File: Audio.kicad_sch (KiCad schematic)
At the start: 8 parts, among them T1 1:1 600R Audio, T2 1:1 600R Audio

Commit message: Assign footprints to devices
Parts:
- C10, C7, C8, C9: footprint (none) -> Capacitor_SMD:C_0201_0603Metric
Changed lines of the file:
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@@
 			)
 		)
-		(property "Footprint" ""
+		(property "Footprint" "Capacitor_SMD:C_0201_0603Metric"
 			(at 162.2552 106.68 0)
 			(effects
@@
 			)
 		)
-		(property "Footprint" ""
+		(property "Footprint" "Capacitor_SMD:C_0201_0603Metric"
 			(at 163.5252 46.99 0)
 			(effects
@@
 			)
 		)
-		(property "Footprint" ""
+		(property "Footprint" "Capacitor_SMD:C_0201_0603Metric"
 			(at 82.55 113.3348 0)
 			(effects
@@
 			)
 		)
-		(property "Footprint" ""
+		(property "Footprint" "Capacitor_SMD:C_0201_0603Metric"
 			(at 97.79 57.15 0)
 			(effects

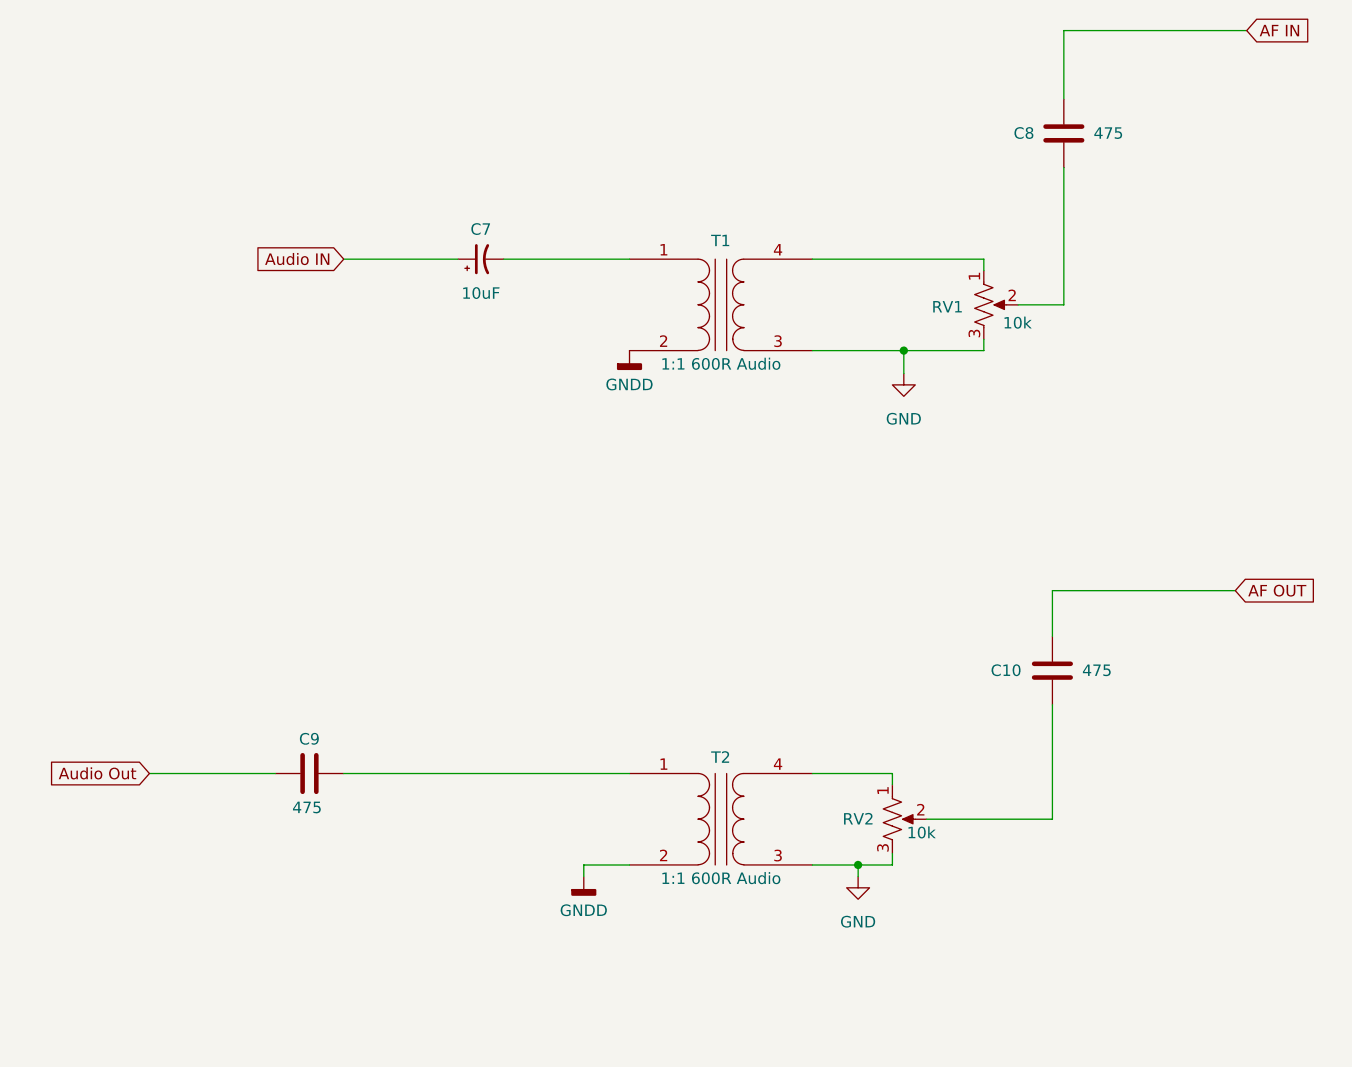
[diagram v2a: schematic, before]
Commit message: Place Audio tranformers and cleanup routing.    Re-annotate based on geographical layout.
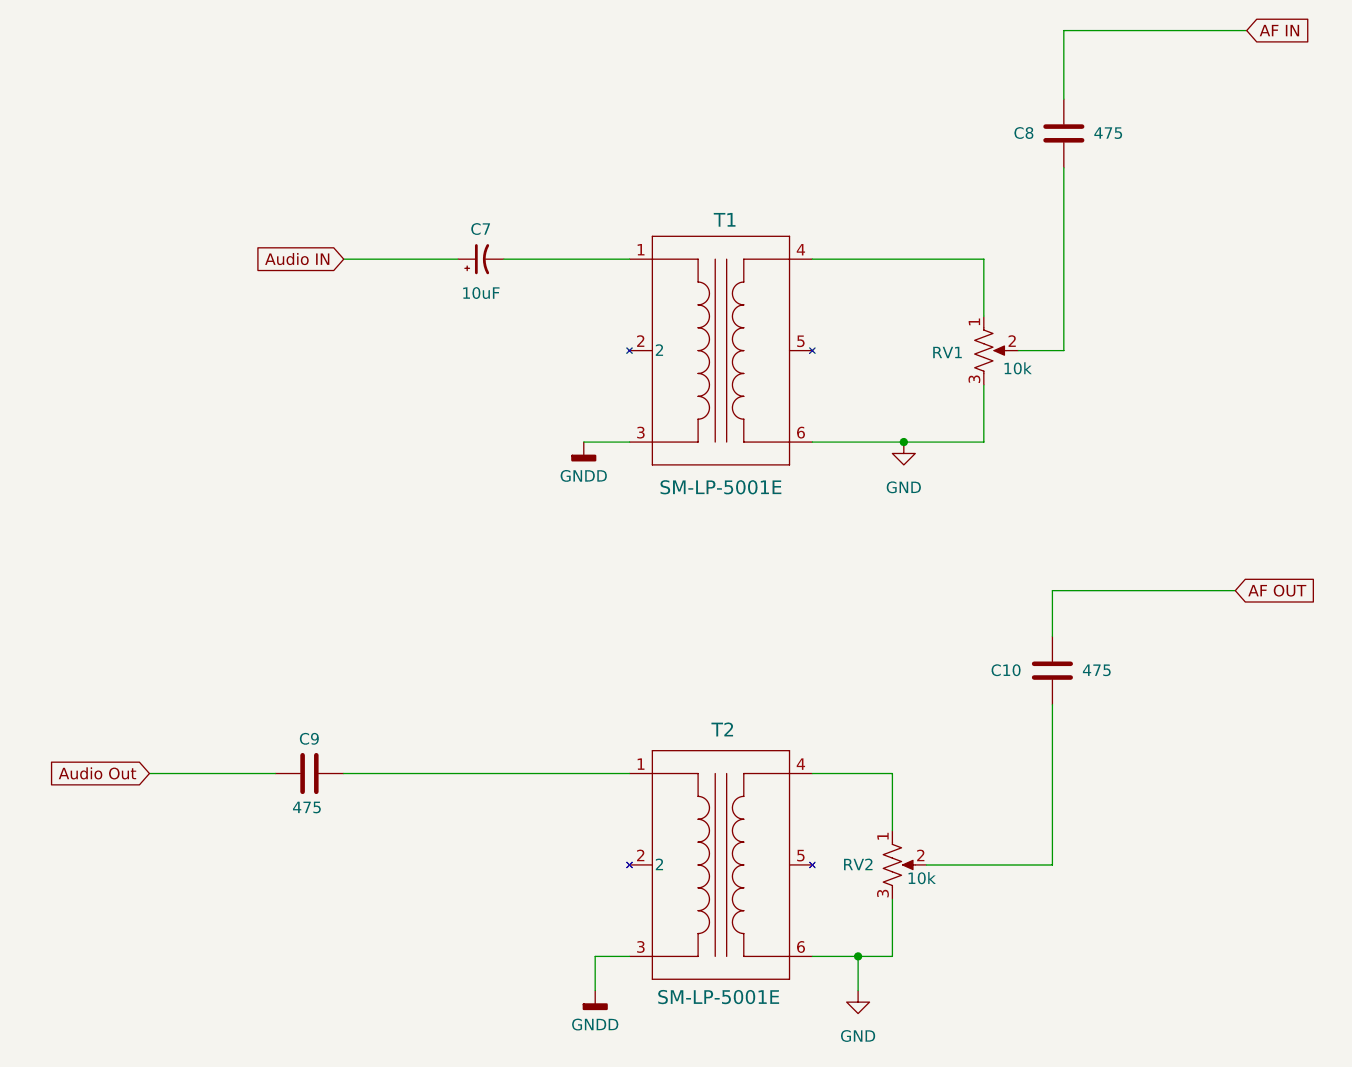
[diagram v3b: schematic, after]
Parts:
- RV1, RV2: footprint (none) -> Potentiometer_SMD:Potentiometer_ACP_CA6-VSMD_Vertical
- T1, T2: value 1:1 600R Audio -> SM-LP-5001E; footprint (none) -> Project_Library:RES6_SM-LP-5001E_BRN-L; symbol Device:Transformer_1P_1S -> Project_Library:SM-LP-5001E
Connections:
- net GND: now also T1.6, T2.6; no longer T1.3 (SA), T2.3 (SA)
- net GNDD: now also T1.3, T2.3; no longer T1.2 (AB), T2.2 (AB)
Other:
- moved on the sheet: RV1, RV2

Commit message: Move Radio interface onto it's own sheet, Add mounting holes and case outline
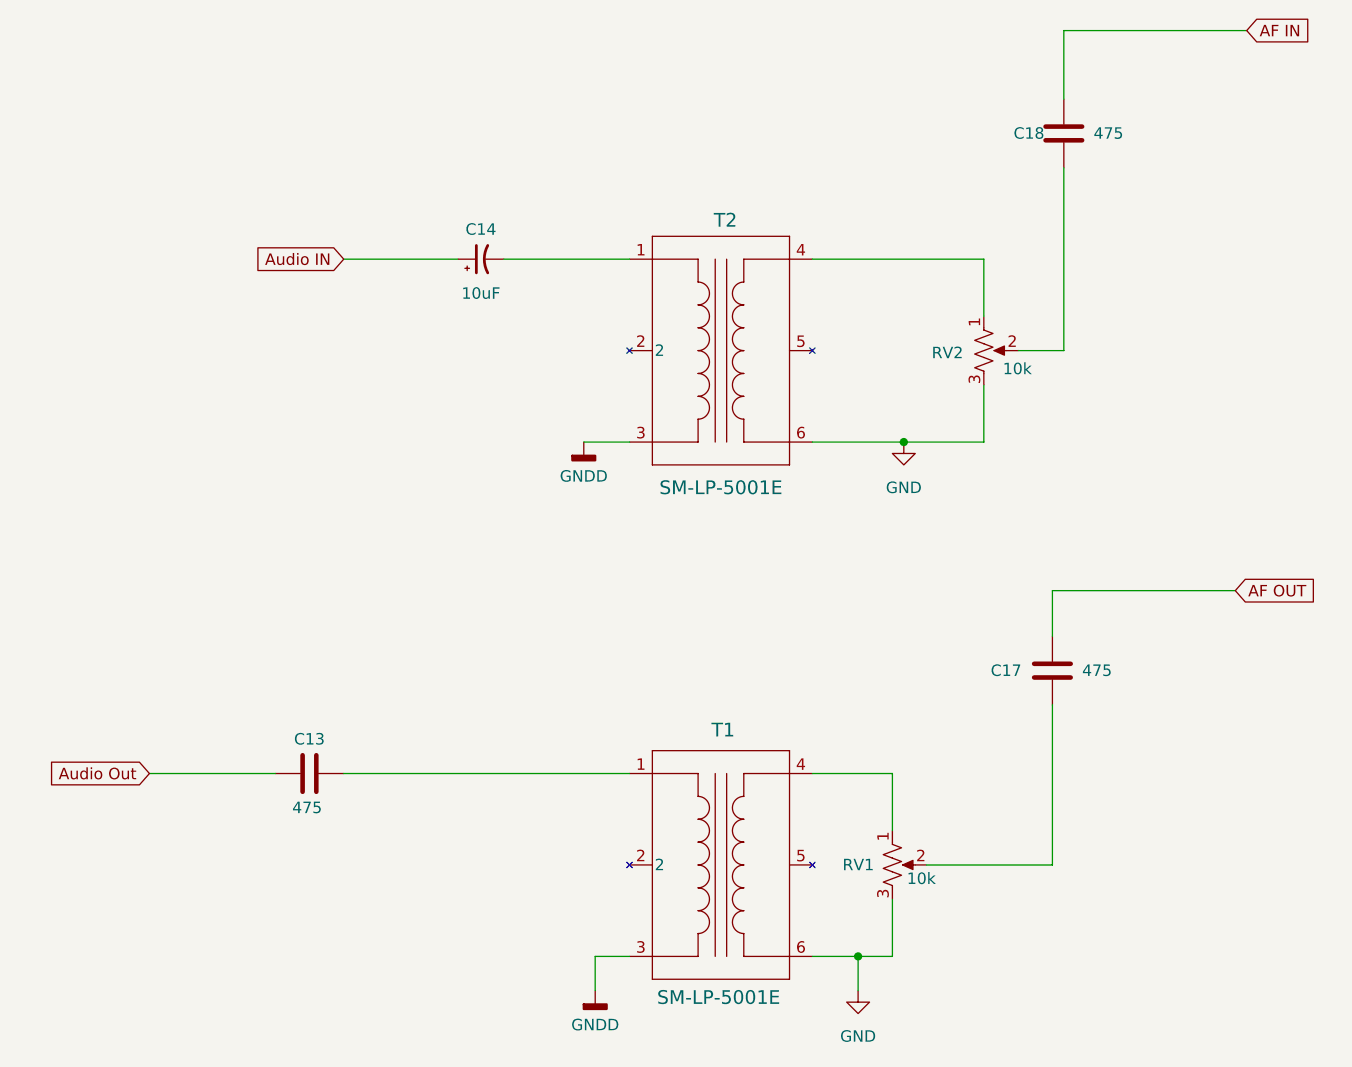
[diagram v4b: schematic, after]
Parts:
- renumbered C9 to C13, C7 to C14, C10 to C17, C8 to C18, RV2 to RV1, RV1 to RV2, T2 to T1, T1 to T2
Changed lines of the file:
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@@
 		(on_board yes)
 		(dnp no)
-		(property "Reference" "C10"
+		(property "Reference" "C17"
 			(at 154.432 102.87 0)
 			(effects
@@
 			(project "digital-mode-radio-interface"
 				(path "/a0d4bcf6-6cac-4e92-853e-9083f008b231/a62d7506-fe91-4265-bb9c-b5dde38a678b"
-					(reference "C10")
+					(reference "C17")
 					(unit 1)
 				)
@@
 		(on_board yes)
 		(dnp no)
-		(property "Reference" "C8"
+		(property "Reference" "C18"
 			(at 156.972 43.18 0)
 			(effects
@@
 			(project "digital-mode-radio-interface"
 				(path "/a0d4bcf6-6cac-4e92-853e-9083f008b231/a62d7506-fe91-4265-bb9c-b5dde38a678b"
-					(reference "C8")
+					(reference "C18")
 					(unit 1)
 				)
@@
 		(on_board yes)
 		(dnp no)
-		(property "Reference" "T2"
+		(property "Reference" "T1"
 			(at 124.714 109.474 0)
 			(effects
@@
 			(project "digital-mode-radio-interface"
 				(path "/a0d4bcf6-6cac-4e92-853e-9083f008b231/a62d7506-fe91-4265-bb9c-b5dde38a678b"
-					(reference "T2")
+					(reference "T1")
 					(unit 1)
 				)
@@
 		(on_board yes)
 		(dnp no)
-		(property "Reference" "C9"
+		(property "Reference" "C13"
 			(at 78.74 110.49 90)
 			(effects
@@
 			(project "digital-mode-radio-interface"
 				(path "/a0d4bcf6-6cac-4e92-853e-9083f008b231/a62d7506-fe91-4265-bb9c-b5dde38a678b"
-					(reference "C9")
+					(reference "C13")
 					(unit 1)
 				)
@@
 		(on_board yes)
 		(dnp no)
-		(property "Reference" "T1"
+		(property "Reference" "T2"
 			(at 124.968 52.832 0)
 			(effects
@@
 			(project "digital-mode-radio-interface"
 				(path "/a0d4bcf6-6cac-4e92-853e-9083f008b231/a62d7506-fe91-4265-bb9c-b5dde38a678b"
-					(reference "T1")
+					(reference "T2")
 					(unit 1)
 				)
@@
 		(on_board yes)
 		(dnp no)
-		(property "Reference" "RV1"
+		(property "Reference" "RV2"
 			(at 151.384 67.564 0)
 			(effects
@@
 			(project "digital-mode-radio-interface"
 				(path "/a0d4bcf6-6cac-4e92-853e-9083f008b231/a62d7506-fe91-4265-bb9c-b5dde38a678b"
-					(reference "RV1")
+					(reference "RV2")
 					(unit 1)
 				)
@@
 		(on_board yes)
 		(dnp no)
-		(property "Reference" "RV2"
+		(property "Reference" "RV1"
 			(at 141.478 124.46 0)
 			(effects
@@
 			(project "digital-mode-radio-interface"
 				(path "/a0d4bcf6-6cac-4e92-853e-9083f008b231/a62d7506-fe91-4265-bb9c-b5dde38a678b"
-					(reference "RV2")
+					(reference "RV1")
 					(unit 1)
 				)
@@
 		(on_board yes)
 		(dnp no)
-		(property "Reference" "C7"
+		(property "Reference" "C14"
 			(at 97.79 53.848 90)
 			(effects
@@
 			(project "digital-mode-radio-interface"
 				(path "/a0d4bcf6-6cac-4e92-853e-9083f008b231/a62d7506-fe91-4265-bb9c-b5dde38a678b"
-					(reference "C7")
-					(unit 1)
-				)
+					(reference "C14")
+					(unit 1)
+				)

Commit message: kiCAD 9.0
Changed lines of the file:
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@@
 (kicad_sch
-	(version 20231120)
+	(version 20250114)
 	(generator "eeschema")
-	(generator_version "8.0")
+	(generator_version "9.0")
 	(paper "USLetter")
 	(title_block
